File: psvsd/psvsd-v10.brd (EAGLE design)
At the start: 30 x 26.8 mm, 28 parts, among them J1 TRANSFLASH-PUSH, U1 USB2244QFN, U3 VREG, Y1 24.000MHz

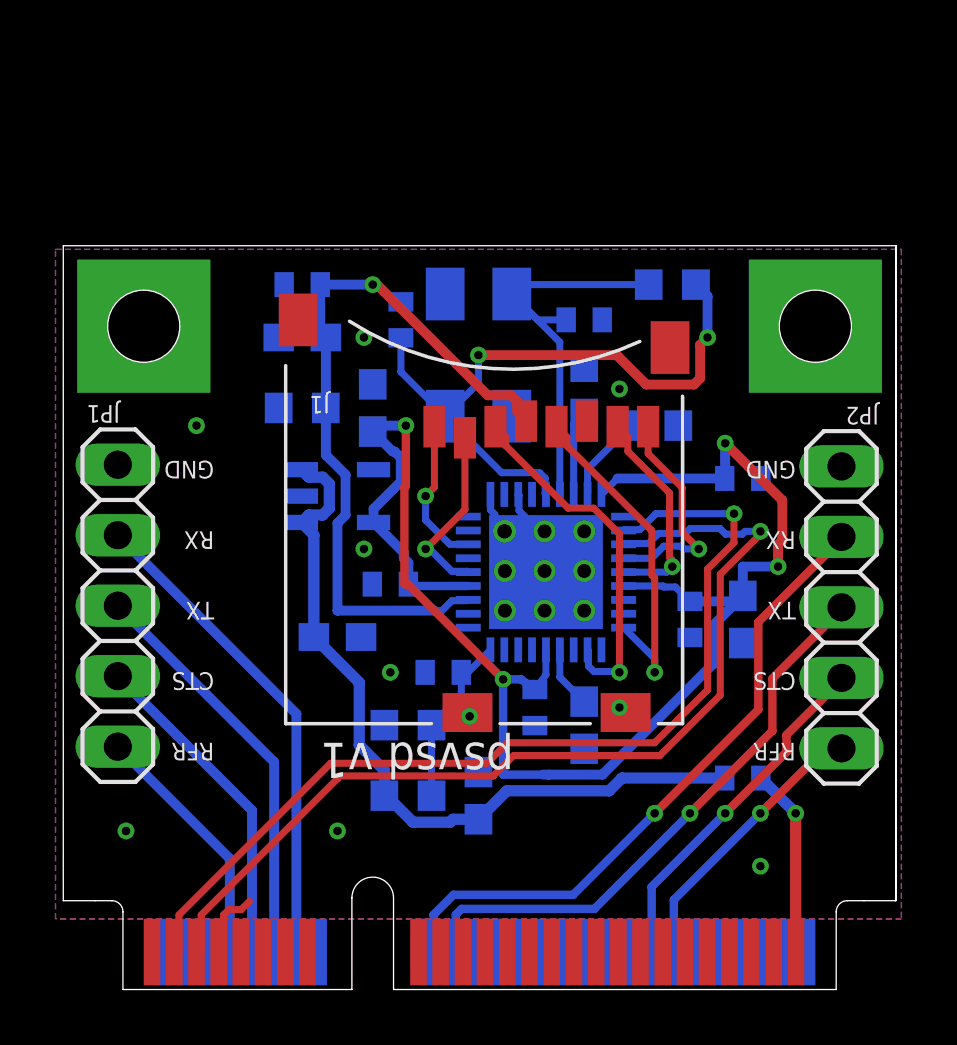
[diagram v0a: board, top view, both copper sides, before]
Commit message: Fixed USB+/USB- signal in psvsd
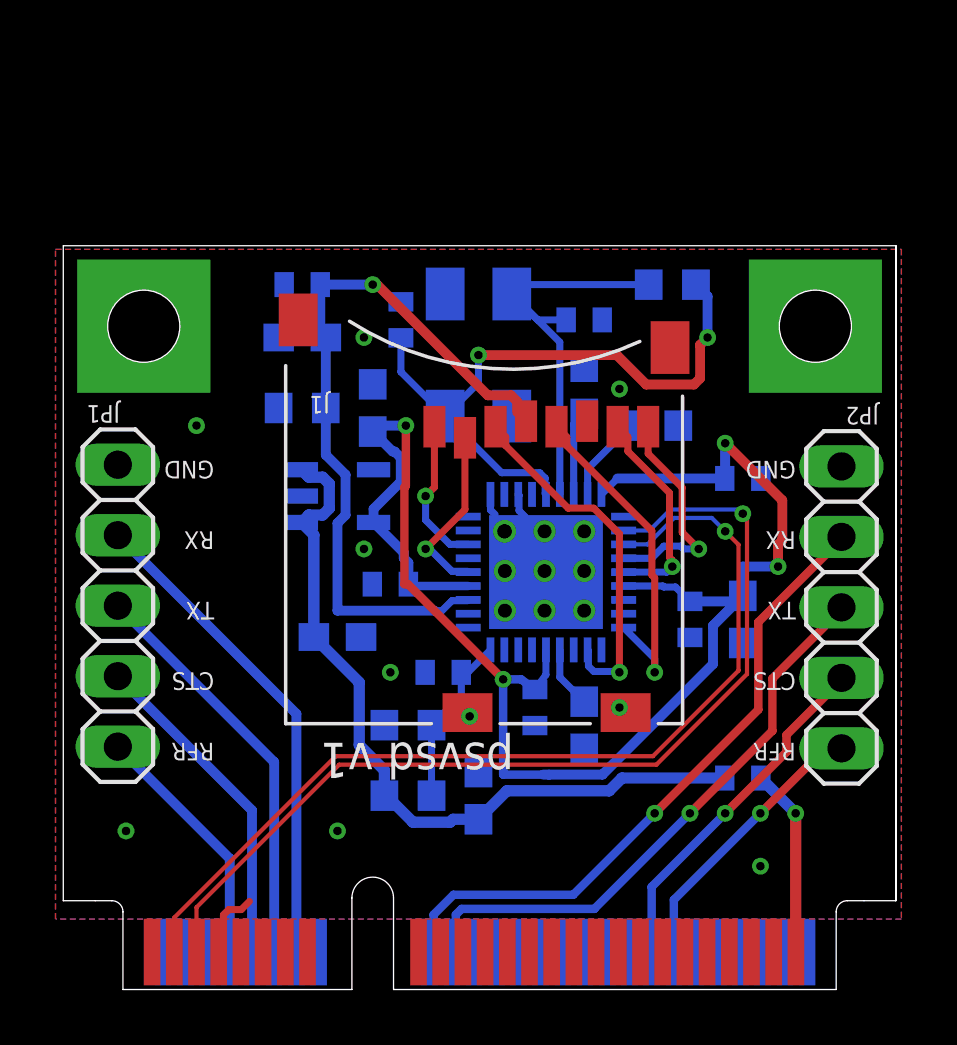
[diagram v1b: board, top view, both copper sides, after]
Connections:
- removed net USB+: U$1.3, U1.2
- removed net USB-: U$1.5, U1.3
- new net USB_N: U$1.3, U1.3
- new net USB_P: U$1.5, U1.2
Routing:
- net USB_P: track 0.00 -> 35.4 mm, vias 0 -> 1
- net USB-: track 35.2 -> 0.00 mm, vias 1 -> 0
- net USB+: track 34.8 -> 0.00 mm, vias 1 -> 0
- net USB_N: track 0.00 -> 34.7 mm, vias 0 -> 1

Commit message: Fixed DRC for new USB lines placement
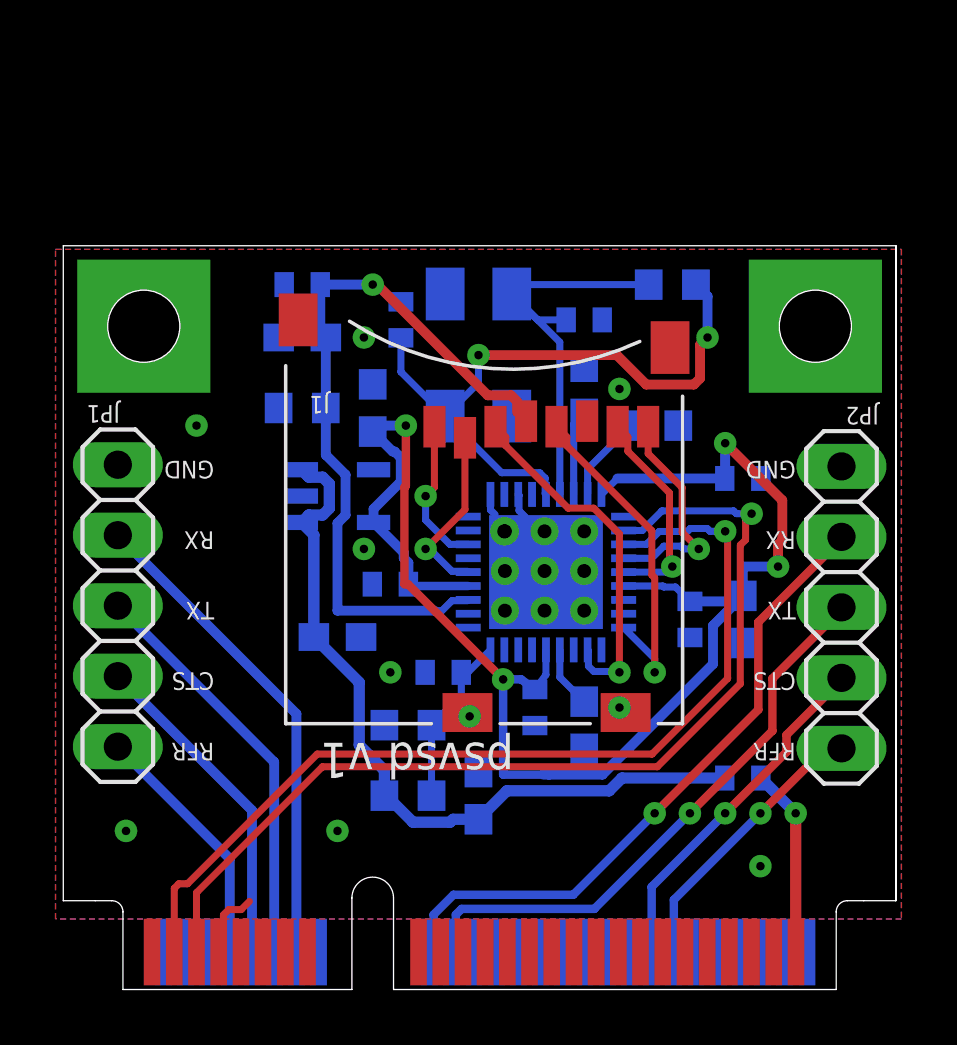
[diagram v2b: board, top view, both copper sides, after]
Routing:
- net USB_P: track 35.4 -> 36.1 mm

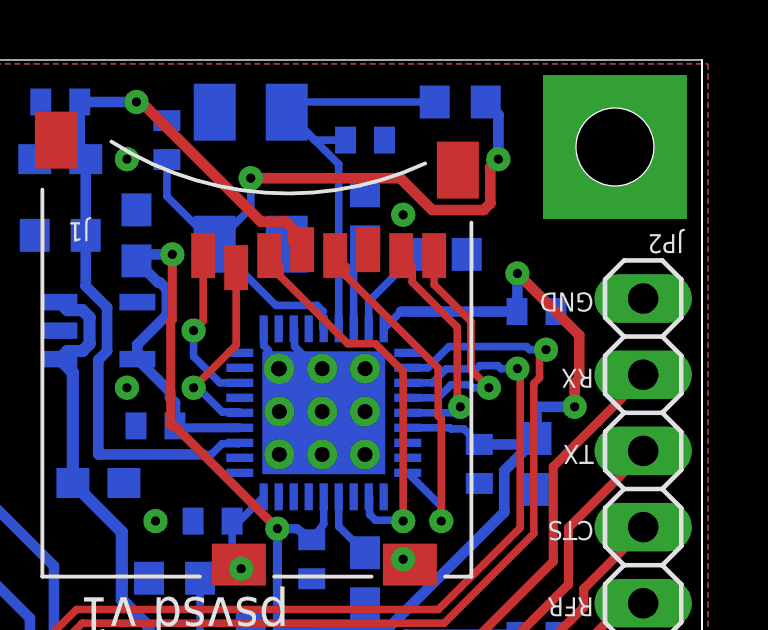
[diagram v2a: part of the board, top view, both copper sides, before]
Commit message: Added LED indicator
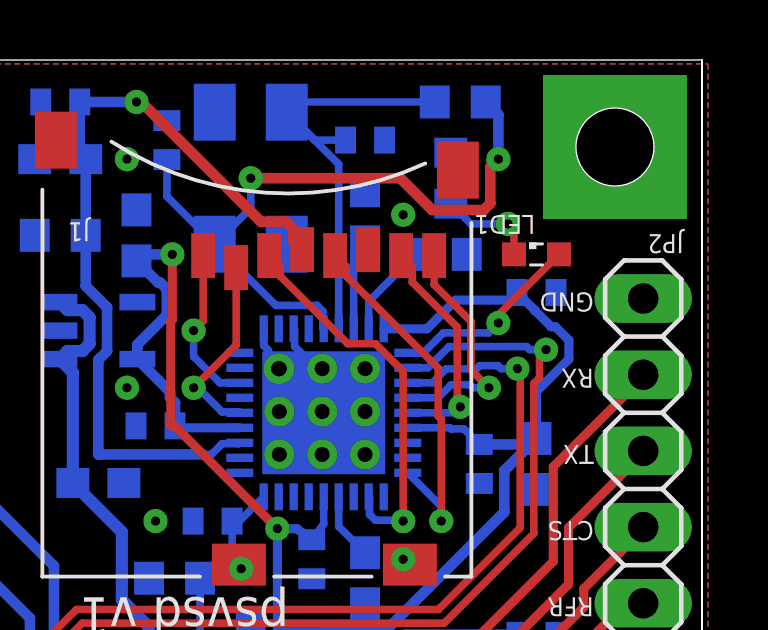
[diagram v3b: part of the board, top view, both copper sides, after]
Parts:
- added LED1: (no value), led:SML0603
- added R6: 1K, rcl:R0603
- moved C12 0.63 mm to (26.0, 21.0)
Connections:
- new net LED: LED1.A, U1.1
- new net N$1: LED1.C, R6.1
- net GND: now also R6.2
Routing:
- net LED: track 0.00 -> 6.56 mm, vias 0 -> 1
- net N$1: track 0.00 -> 3.28 mm, vias 0 -> 1
- net VDD33: track 58.1 -> 55.5 mm, vias 4 -> 2

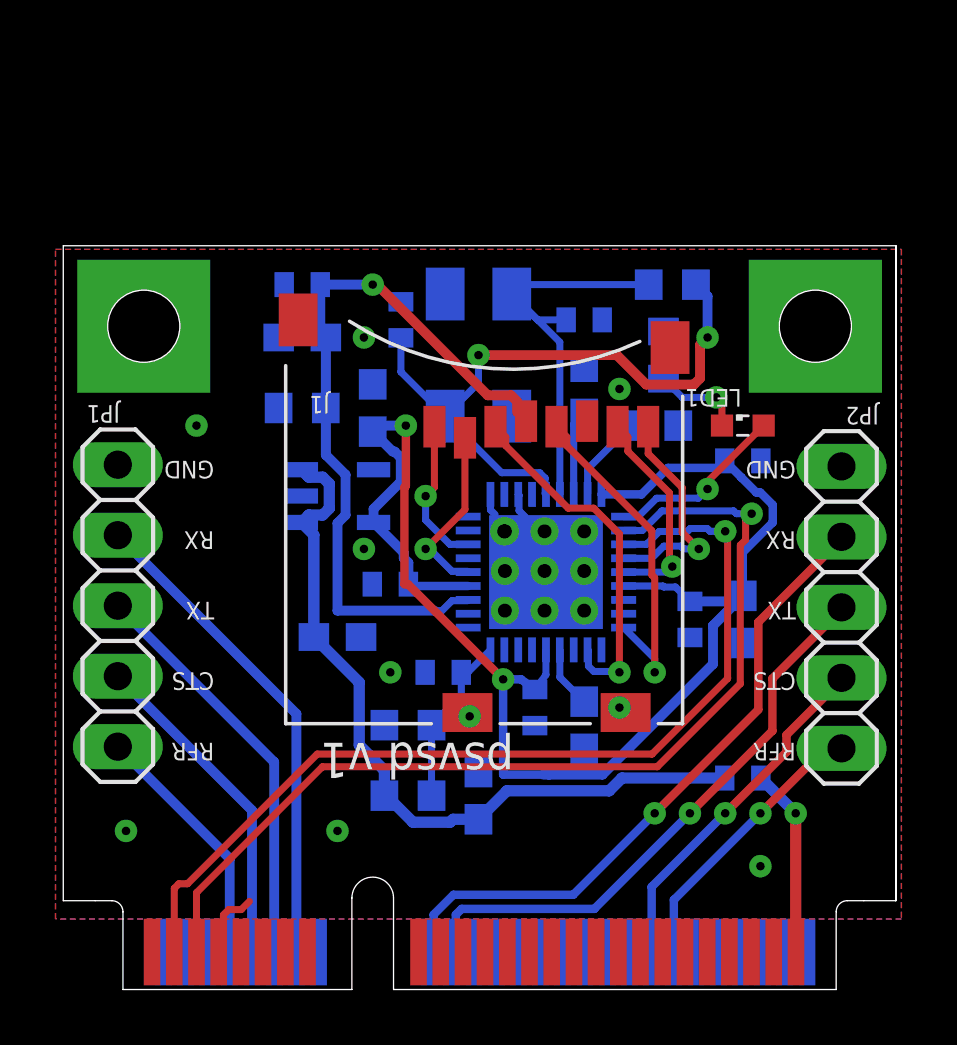
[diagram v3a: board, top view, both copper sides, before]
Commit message: Updated board to be right size
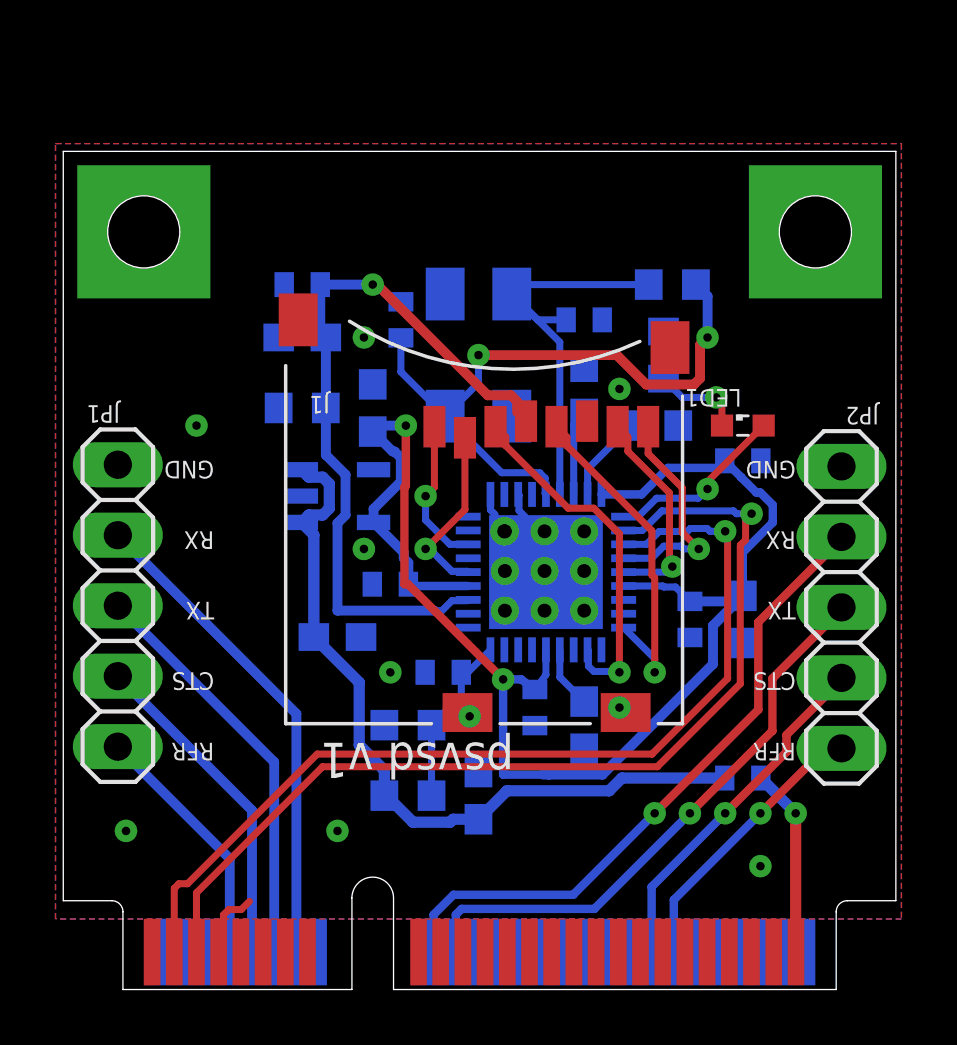
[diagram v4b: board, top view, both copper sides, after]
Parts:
- U$1: device mini-pci-e:HALF-MINI-PCI-E -> mini-pci-e:VITA-MINI-PCI-E
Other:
- board size 30 x 26.8 mm -> 30 x 30.2 mm
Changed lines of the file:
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@@
 <attribute name="NAME" x="11.149" y="23.295" size="0.635" layer="25" rot="SR180"/>
 </element>
-<element name="U$1" library="mini-pci-e" package="HALF-MINI-PCI-E" value="VITA-CUSTOM" x="12.7" y="1.905"/>
+<element name="U$1" library="mini-pci-e" package="VITA-MINI-PCI-E" value="VITA-CUSTOM" x="12.7" y="1.905"/>
 <element name="U1" library="USB2244" package="QFN36" value="USB2244QFN" x="18.942" y="16.945" smashed="yes" rot="MR270">
 <attribute name="NAME" x="21.992" y="14.51" size="0.508" layer="26" rot="MR270"/>
@@
 <via x="20.32" y="15.5575" extent="1-16" drill="0.5" diameter="0.5"/>
 <polygon width="0.254" layer="1">
-<vertex x="1.27" y="28.575"/>
-<vertex x="31.75" y="28.575"/>
+<vertex x="1.27" y="32.385"/>
+<vertex x="31.75" y="32.385"/>
 <vertex x="31.75" y="4.445"/>
 <vertex x="1.27" y="4.445"/>
@@
 <via x="17.4625" y="18.415" extent="1-16" drill="0.5"/>
 <polygon width="0.254" layer="16">
-<vertex x="1.27" y="28.575"/>
-<vertex x="31.75" y="28.575"/>
+<vertex x="1.27" y="32.385"/>
+<vertex x="31.75" y="32.385"/>
 <vertex x="31.75" y="4.445"/>
 <vertex x="1.27" y="4.445"/>

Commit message: Resize both boards
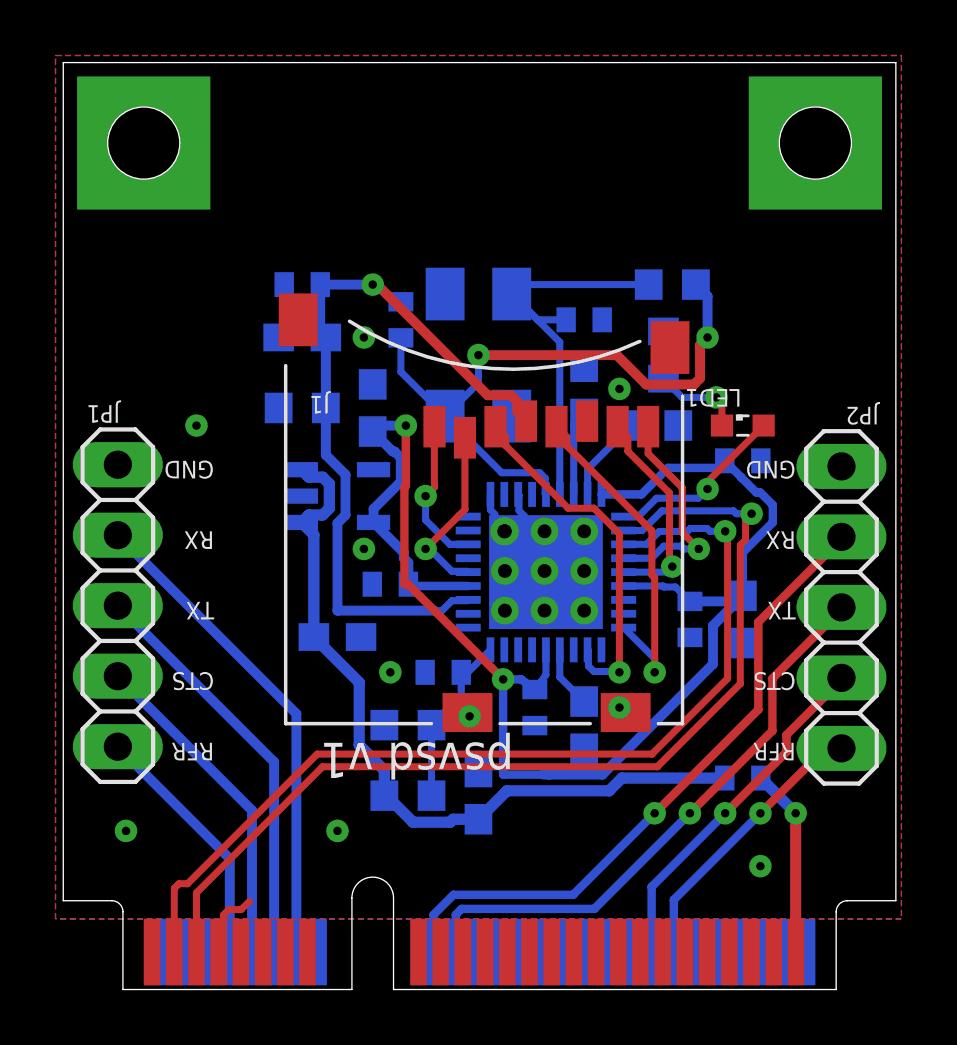
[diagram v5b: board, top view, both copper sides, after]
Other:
- board size 30 x 30.2 mm -> 30 x 33.4 mm
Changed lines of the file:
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@@
 <via x="20.32" y="15.5575" extent="1-16" drill="0.5" diameter="0.5"/>
 <polygon width="0.254" layer="1">
-<vertex x="1.27" y="32.385"/>
-<vertex x="31.75" y="32.385"/>
+<vertex x="1.27" y="35.56"/>
+<vertex x="31.75" y="35.56"/>
 <vertex x="31.75" y="4.445"/>
 <vertex x="1.27" y="4.445"/>
@@
 <via x="17.4625" y="18.415" extent="1-16" drill="0.5"/>
 <polygon width="0.254" layer="16">
-<vertex x="1.27" y="32.385"/>
-<vertex x="31.75" y="32.385"/>
+<vertex x="1.27" y="35.56"/>
+<vertex x="31.75" y="35.56"/>
 <vertex x="31.75" y="4.445"/>
 <vertex x="1.27" y="4.445"/>

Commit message: Shifted all components up in the new space
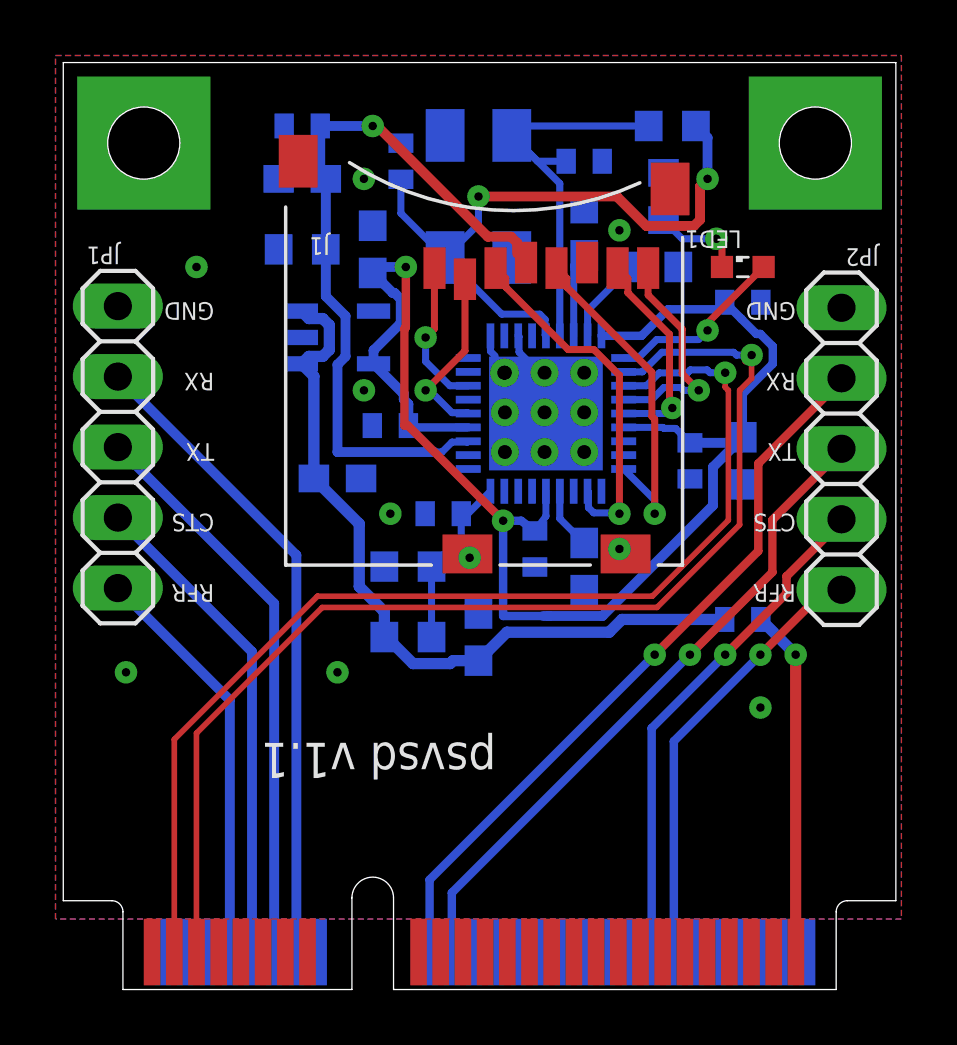
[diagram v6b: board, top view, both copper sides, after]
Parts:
- moved C12 5.72 mm to (26.0, 26.7)
- moved C15 5.72 mm to (10.2, 33.0)
- moved R1 5.72 mm to (23.5, 33.0)
- moved C11 5.72 mm to (18.5, 17.8)
- moved C1 5.71 mm to (11.4, 20.3)
- moved C13 5.71 mm to (13.3, 22.2)
- moved C14 5.71 mm to (10.2, 31.1)
- moved C2 5.71 mm to (12.7, 28.6)
- moved C3 5.71 mm to (20.3, 31.8)
- moved C4 5.71 mm to (13.7, 31.8)
- moved C5 5.71 mm to (16.5, 14.6)
- moved C6 5.71 mm to (15.2, 19.1)
- moved C7 5.71 mm to (20.3, 29.2)
- moved C8 5.71 mm to (20.3, 17.1)
- moved FB1 5.71 mm to (26.0, 15.2)
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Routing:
- net USB_P: track 36.1 -> 42.1 mm
- net UART_SYSCON_RFR: track 12.7 -> 18.4 mm
- net UART_KERMIT_RX: track 17.7 -> 23.4 mm
- net +5V: track 6.85 -> 12.6 mm
- net UART_KERMIT_TX: track 14.8 -> 20.5 mm
- net UART_KERMIT_RFR: track 9.07 -> 14.8 mm
- net UART_KERMIT_CTS: track 11.9 -> 17.7 mm
- net UART_SYSCON_CTS: track 10.2 -> 15.9 mm
- net USB_N: track 34.6 -> 40.3 mm
- net UART_SYSCON_RX: track 23.6 -> 27.0 mm
- net UART_SYSCON_TX: track 21.0 -> 24.2 mm
- net GND: track 5.50 -> 3.20 mm
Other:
- board text added: "psvsd v1.1"
- board text removed: "psvsd v1"
